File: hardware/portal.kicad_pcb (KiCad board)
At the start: 2 copper layers, 56.5 x 67 mm, 19 parts, among them J1 Screw_Terminal_1x02, J10 Screw_Terminal_1x02, J11 Screw_Terminal_1x02, J2 Screw_Terminal_1x02, J3 Raspberry_Pi_2_3, J4 CONN_01X01, J5 CONN_01X01, J6 CONN_01X01, J7 CONN_01X01, J8 Screw_Terminal_1x02, U1 PC817, U2 PC817

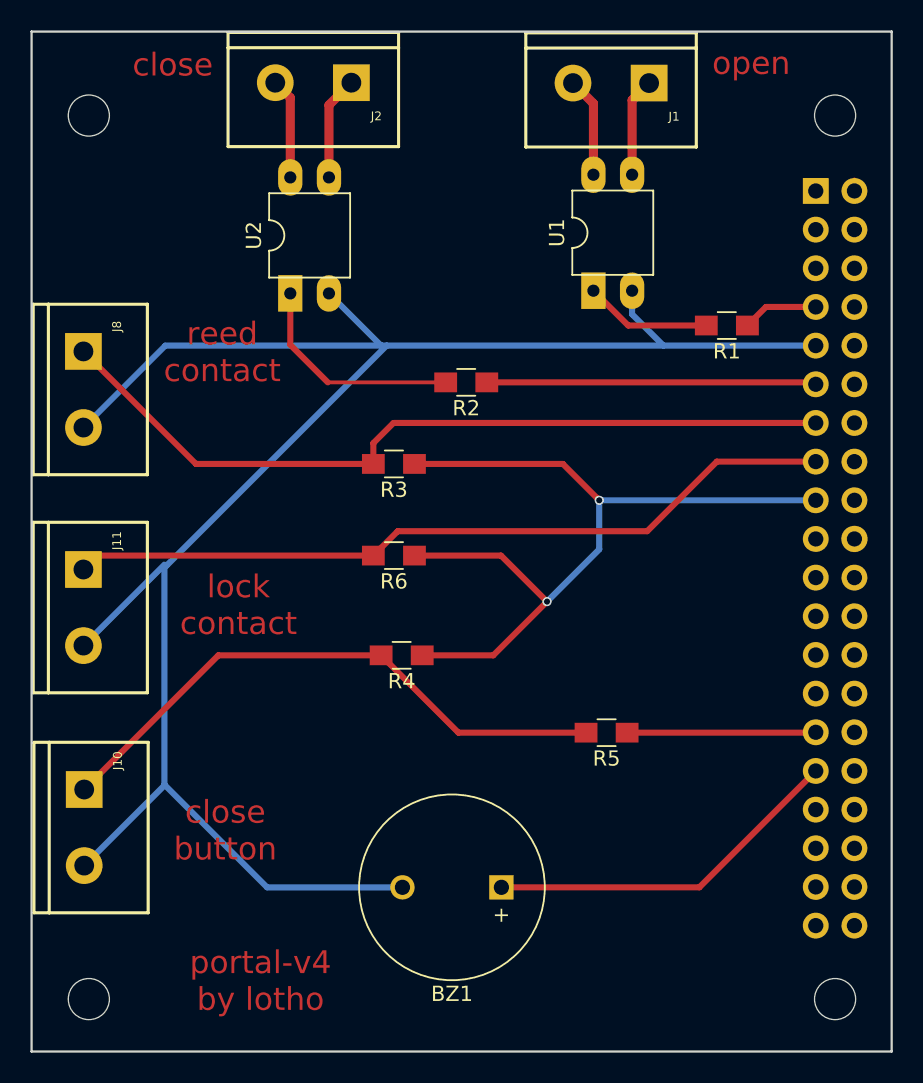
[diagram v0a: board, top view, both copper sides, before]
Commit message: Added debouncing to the PCB and widened the traces
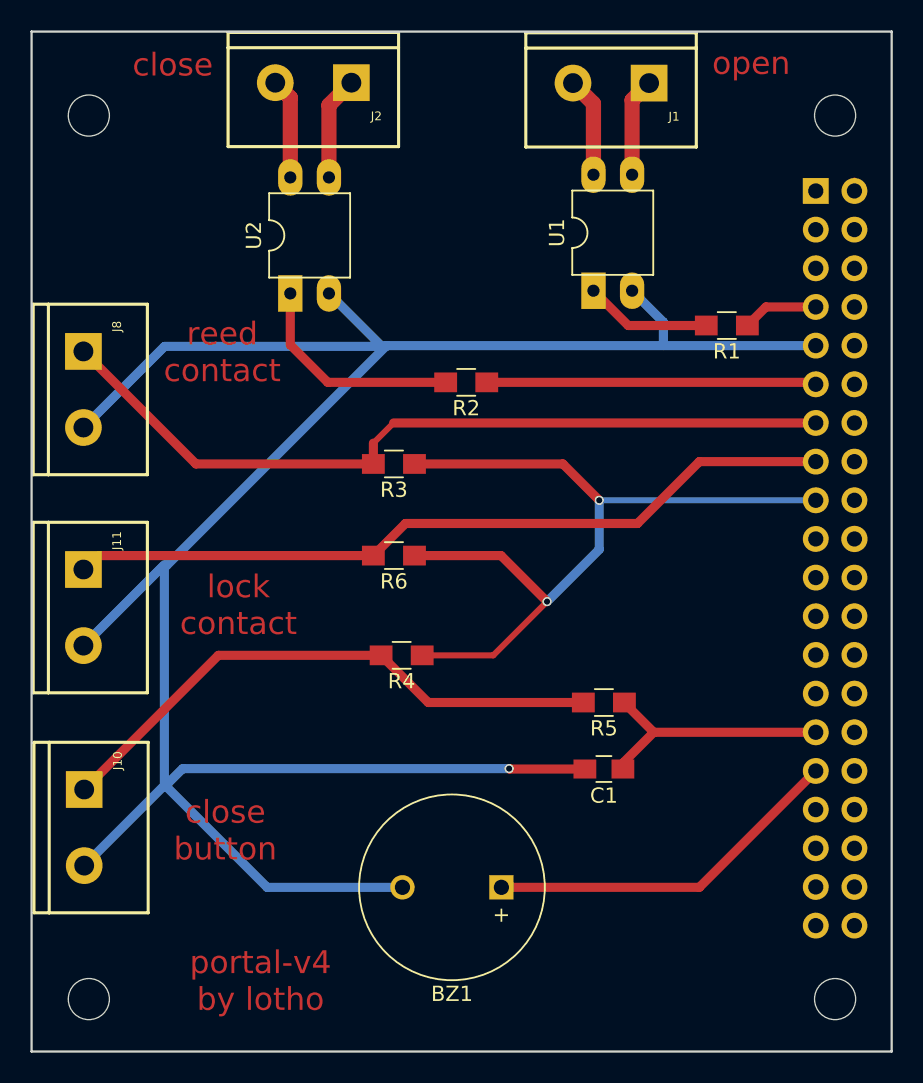
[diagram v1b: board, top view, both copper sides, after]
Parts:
- added C1: 220nF, Capacitors_SMD:C_0805_HandSoldering, F.Cu at (153.6, 107.4)
- moved R5 1.99 mm to (153.6, 103.1)
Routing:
- net GND: track 128.3 -> 156.6 mm, vias 0 -> 1
- net /closebutton: track 12.4 -> 17.0 mm
- net Net-(J1-Pad1): track 6.48 -> 8.06 mm
- net Net-(J10-Pad1): track 38.7 -> 37.7 mm
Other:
- net class Default: trace_width 0.4 -> 0.6
- net class more power: trace_width 0.6 -> 1
